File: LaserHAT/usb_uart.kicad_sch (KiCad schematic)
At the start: 9 parts

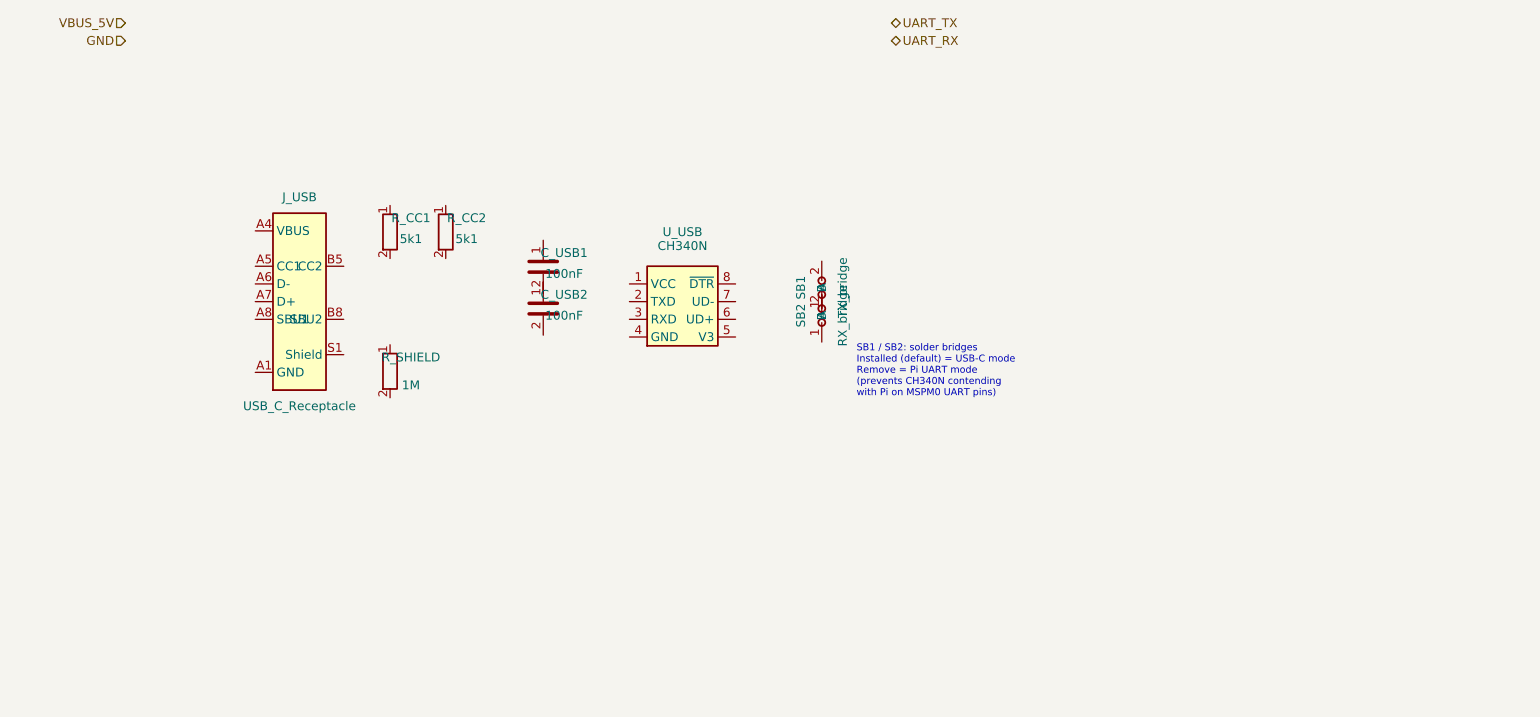
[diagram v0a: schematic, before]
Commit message: Regenerate schematics via kiutils; add generate_schematics.py
Previous hand-written schematics failed to open in eeschema due to
quoted UUIDs and unrecognised generator_version field.  Replace with
a kiutils-based Python generator that produces correctly-formatted
KiCad 9 S-expressions.

Each sheet now has:
- Unquoted UUIDs and proper PageSettings object (eeschema-compatible)
- HierarchicalLabel port declarations matching parent sheet pins
- LocalLabel net labels placed at exact pin connection points so KiCad
  can build the netlist without manual wire routing
- NoConnect markers on unused pins (SBU1/SBU2, DTR, MT3608 NC pin)
- SymbolInstance entries for BOM/netlist annotation

Add requirements.txt (kiutils==1.4.8) for reproducible environment.

Run: .venv/bin/python3 LaserHAT/generate_schematics.py

Co-Authored-By: Claude Sonnet 4.6 <noreply@anthropic.com>
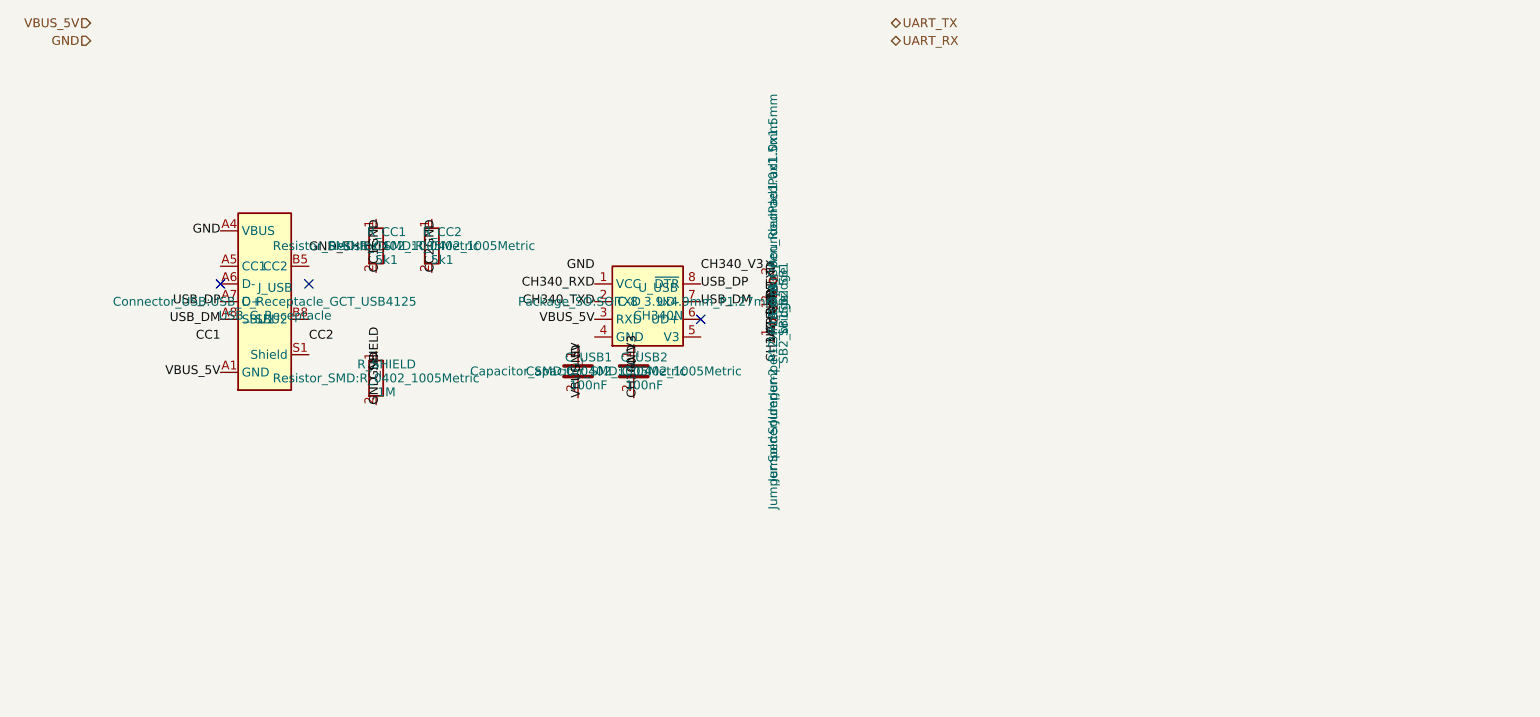
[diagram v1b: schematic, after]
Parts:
- SB1: value TX_bridge -> SB1_bridge
- SB2: value RX_bridge -> SB2_bridge
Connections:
- net GND: now also C_USB1.1, C_USB2.1, J_USB.A4 (VBUS), R_CC1.1, R_CC2.1, R_SHIELD.1
- net UART_RX: now also SB2.1 (A)
- net UART_TX: now also SB1.1 (A)
- net VBUS_5V: now also C_USB1.2, J_USB.A1 (GND), U_USB.3 (RXD)
- net USB_DP: now reaches J_USB.A7 (D+)
- net USB_DP: now also U_USB.8 (~{DTR})
- net USB_DM: now reaches J_USB.A8 (SBU1)
- net USB_DM: now also U_USB.7 (UD-)
- net CC1: now reaches R_CC1.2
- net CC2: now reaches R_CC2.2
- net GND_SHIELD: now reaches R_SHIELD.2
- net CH340_V3: now reaches C_USB2.2
- net CH340_RXD: now reaches U_USB.1 (VCC)
- net CH340_RXD: now also SB2.2 (B)
- net CH340_TXD: now reaches U_USB.2 (TXD)
- net CH340_TXD: now also SB1.2 (B)
- no-connect marks 0 -> 3
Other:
- note removed: "SB1 / SB2: solder bridges Installed (default) = USB-C mode Remove = Pi UART mode (prevents CH340N contending with Pi on MSPM0 UART pins)"

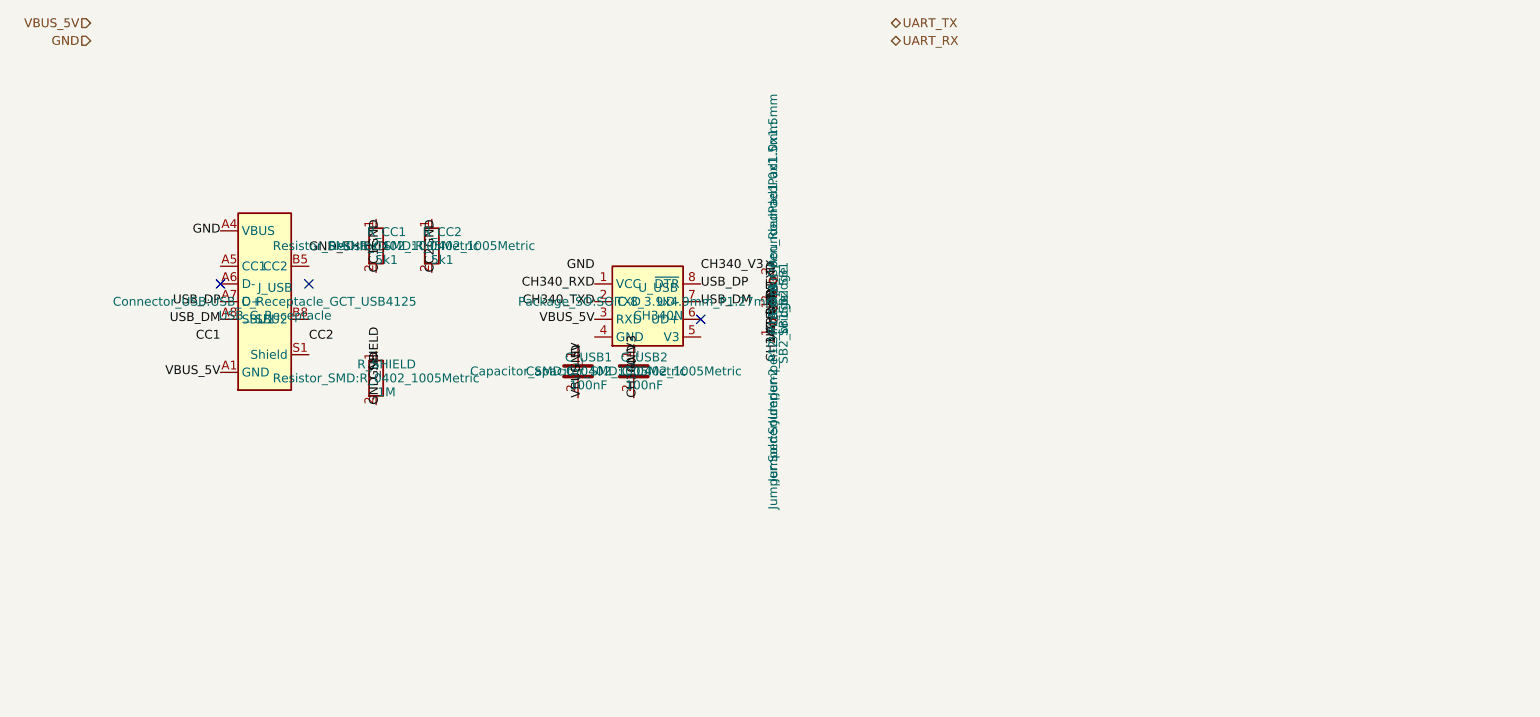
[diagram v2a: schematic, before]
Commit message: Implement schematic design rules; add CLAUDE.md
- Rule 1: hide pin names/numbers on passive parts (R, C, L)
- Rule 2: add ≥5mm wire stub before every net label
- Rule 3: preserve hand-edited laser_driver.kicad_sch by loading from PCB/ original
- Rule 4: generous component spacing across multiple sheets
- Add CLAUDE.md documenting all rules, setup, signal naming, and kiutils conventions

Co-Authored-By: Claude Sonnet 4.6 <noreply@anthropic.com>
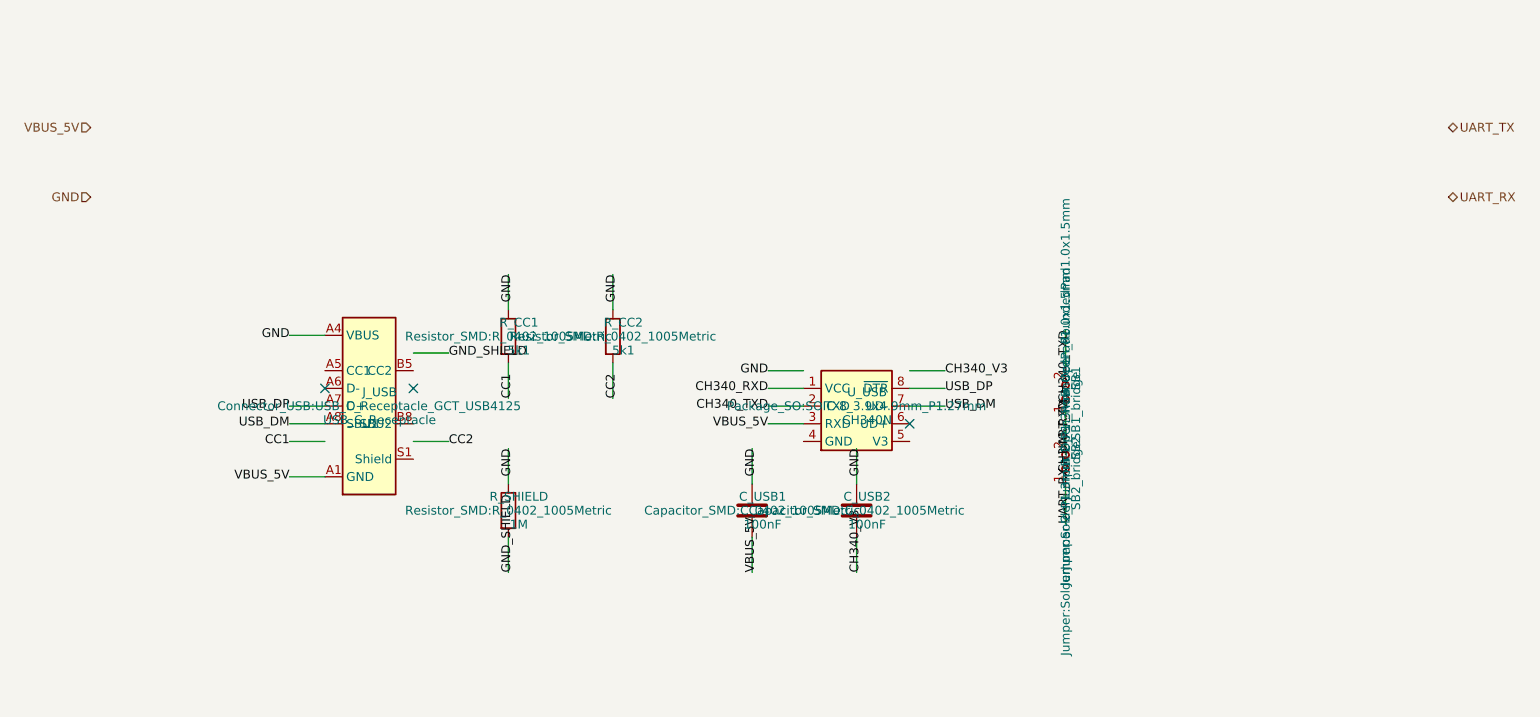
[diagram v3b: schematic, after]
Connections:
- net CH340_RXD is gone; now on net UART_TX: SB2.2 (B), U_USB.1 (VCC)

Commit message: Fix three schematic generation bugs
- Symbol unit names: set entryName on manually-created Symbol units so
  they serialize as "+LASER_V_0_1" not "None_0_1" (KiCad load error)
- Passive pin hiding: set pinNames=True alongside pinNamesHide=True so
  the (pin_names hide) token is actually emitted for Device:C and Device:L
- Property visibility: hide Footprint/Datasheet/Description on all
  schematic symbol instances; only Reference and Value remain shown

Co-Authored-By: Claude Sonnet 4.6 <noreply@anthropic.com>
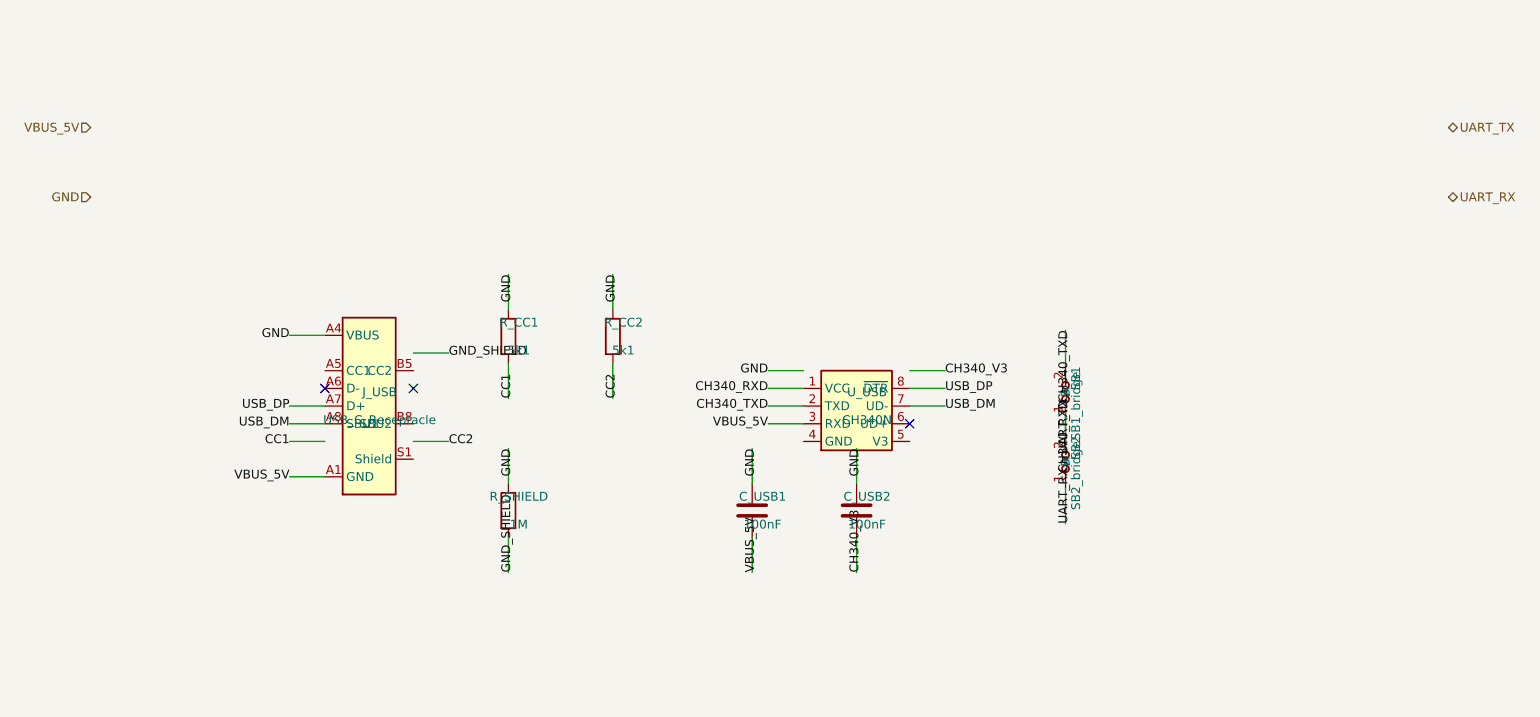
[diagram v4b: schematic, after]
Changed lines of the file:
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@@
     )
     (property "Footprint" "Connector_USB:USB_C_Receptacle_GCT_USB4125" (at 45 60 0)
-      (effects (font (size 1.27 1.27)))
+      (effects (font (size 1.27 1.27)) hide)
     )
     (property "Datasheet" "~" (at 45 60 0)
-      (effects (font (size 1.27 1.27)))
+      (effects (font (size 1.27 1.27)) hide)
     )
     (pin "A4")
@@
     )
     (property "Footprint" "Resistor_SMD:R_0402_1005Metric" (at 65 50 0)
-      (effects (font (size 1.27 1.27)))
+      (effects (font (size 1.27 1.27)) hide)
     )
     (property "Datasheet" "~" (at 65 50 0)
-      (effects (font (size 1.27 1.27)))
+      (effects (font (size 1.27 1.27)) hide)
     )
     (pin "1")
@@
     )
     (property "Footprint" "Resistor_SMD:R_0402_1005Metric" (at 80 50 0)
-      (effects (font (size 1.27 1.27)))
+      (effects (font (size 1.27 1.27)) hide)
     )
     (property "Datasheet" "~" (at 80 50 0)
-      (effects (font (size 1.27 1.27)))
+      (effects (font (size 1.27 1.27)) hide)
     )
     (pin "1")
@@
     )
     (property "Footprint" "Resistor_SMD:R_0402_1005Metric" (at 65 75 0)
-      (effects (font (size 1.27 1.27)))
+      (effects (font (size 1.27 1.27)) hide)
     )
     (property "Datasheet" "~" (at 65 75 0)
-      (effects (font (size 1.27 1.27)))
+      (effects (font (size 1.27 1.27)) hide)
     )
     (pin "1")
@@
     )
     (property "Footprint" "Package_SO:SOIC-8_3.9x4.9mm_P1.27mm" (at 115 60 0)
-      (effects (font (size 1.27 1.27)))
+      (effects (font (size 1.27 1.27)) hide)
     )
     (property "Datasheet" "~" (at 115 60 0)
-      (effects (font (size 1.27 1.27)))
+      (effects (font (size 1.27 1.27)) hide)
     )
     (pin "1")
@@
     )
     (property "Footprint" "Capacitor_SMD:C_0402_1005Metric" (at 100 75 0)
-      (effects (font (size 1.27 1.27)))
+      (effects (font (size 1.27 1.27)) hide)
     )
     (property "Datasheet" "~" (at 100 75 0)
-      (effects (font (size 1.27 1.27)))
+      (effects (font (size 1.27 1.27)) hide)
     )
     (pin "1")
@@
     )
     (property "Footprint" "Capacitor_SMD:C_0402_1005Metric" (at 115 75 0)
-      (effects (font (size 1.27 1.27)))
+      (effects (font (size 1.27 1.27)) hide)
     )
     (property "Datasheet" "~" (at 115 75 0)
-      (effects (font (size 1.27 1.27)))
+      (effects (font (size 1.27 1.27)) hide)
     )
     (pin "1")
@@
     )
     (property "Footprint" "Jumper:SolderJumper-2_P1.3mm_Open_RoundedPad1.0x1.5mm" (at 145 58 0)
-      (effects (font (size 1.27 1.27)))
+      (effects (font (size 1.27 1.27)) hide)
     )
     (property "Datasheet" "~" (at 145 58 0)
-      (effects (font (size 1.27 1.27)))
+      (effects (font (size 1.27 1.27)) hide)
     )
     (pin "1")
@@
     )
     (property "Footprint" "Jumper:SolderJumper-2_P1.3mm_Open_RoundedPad1.0x1.5mm" (at 145 68 0)
-      (effects (font (size 1.27 1.27)))
+      (effects (font (size 1.27 1.27)) hide)
     )
     (property "Datasheet" "~" (at 145 68 0)
-      (effects (font (size 1.27 1.27)))
+      (effects (font (size 1.27 1.27)) hide)
     )
     (pin "1")
@@
   )
   (symbol_instances
-    (path "/212bfd25-f831-4b85-926b-000000000004/e0ca20b7-23f3-4424-aec8-fc5ed807df41"
+    (path "/212bfd25-f831-4b85-926b-000000000004/50dc2b85-6e56-463d-938c-c9b5e5251356"
       (reference "J_USB") (unit 1) (value "USB_C_Receptacle") (footprint "Connector_USB:USB_C_Receptacle_GCT_USB4125")
     )
-    (path "/212bfd25-f831-4b85-926b-000000000004/6990e763-b4ba-488b-9920-c4500c993b11"
+    (path "/212bfd25-f831-4b85-926b-000000000004/e9dbbd6a-570c-4209-82c4-f676de474bc6"
       (reference "R_CC1") (unit 1) (value "5k1") (footprint "Resistor_SMD:R_0402_1005Metric")
     )
-    (path "/212bfd25-f831-4b85-926b-000000000004/c153a01f-840f-4a4c-ac2e-8bcf8c7cdf24"
+    (path "/212bfd25-f831-4b85-926b-000000000004/c97010d5-b40c-4a1b-8ab2-49e8ee4077aa"
       (reference "R_CC2") (unit 1) (value "5k1") (footprint "Resistor_SMD:R_0402_1005Metric")
     )
-    (path "/212bfd25-f831-4b85-926b-000000000004/8090caf5-55a8-4073-98b8-e9e013e0fb6e"
+    (path "/212bfd25-f831-4b85-926b-000000000004/6643c6db-d436-464e-85c8-bcf5f708e534"
       (reference "R_SHIELD") (unit 1) (value "1M") (footprint "Resistor_SMD:R_0402_1005Metric")
     )
-    (path "/212bfd25-f831-4b85-926b-000000000004/4bd9cb01-8b13-48ba-8b06-8f6e4c2b73e2"
+    (path "/212bfd25-f831-4b85-926b-000000000004/22bd5166-6294-4ac8-9ad9-a0bc21f87446"
       (reference "U_USB") (unit 1) (value "CH340N") (footprint "Package_SO:SOIC-8_3.9x4.9mm_P1.27mm")
     )
-    (path "/212bfd25-f831-4b85-926b-000000000004/ac98e5c8-5793-4cb6-9596-54fb8c49d3ce"
+    (path "/212bfd25-f831-4b85-926b-000000000004/00e72fd9-97d5-4396-965a-ede833e229ab"
       (reference "C_USB1") (unit 1) (value "100nF") (footprint "Capacitor_SMD:C_0402_1005Metric")
     )
-    (path "/212bfd25-f831-4b85-926b-000000000004/357f0027-6be9-456b-a47a-2cde5c65af93"
+    (path "/212bfd25-f831-4b85-926b-000000000004/3160f2aa-1f47-47c4-9b02-5ceb3f61dff5"
       (reference "C_USB2") (unit 1) (value "100nF") (footprint "Capacitor_SMD:C_0402_1005Metric")
     )
-    (path "/212bfd25-f831-4b85-926b-000000000004/d4662d21-efad-4d01-9b5a-e80455919fb2"
+    (path "/212bfd25-f831-4b85-926b-000000000004/15e7e694-8d0e-4f92-ae43-5f42842a6977"
       (reference "SB1") (unit 1) (value "SB1_bridge") (footprint "Jumper:SolderJumper-2_P1.3mm_Open_RoundedPad1.0x1.5mm")
     )
-    (path "/212bfd25-f831-4b85-926b-000000000004/c2977167-c831-47f2-861c-8d4defa2074e"
+    (path "/212bfd25-f831-4b85-926b-000000000004/41149967-97ff-45bb-99a2-b8a2602378f4"
       (reference "SB2") (unit 1) (value "SB2_bridge") (footprint "Jumper:SolderJumper-2_P1.3mm_Open_RoundedPad1.0x1.5mm")
     )
